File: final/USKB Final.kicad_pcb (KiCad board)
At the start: 2 copper layers, 385.8 x 100 mm, 166 parts, among them SW1 SW_PUSH, U1 ProMicro

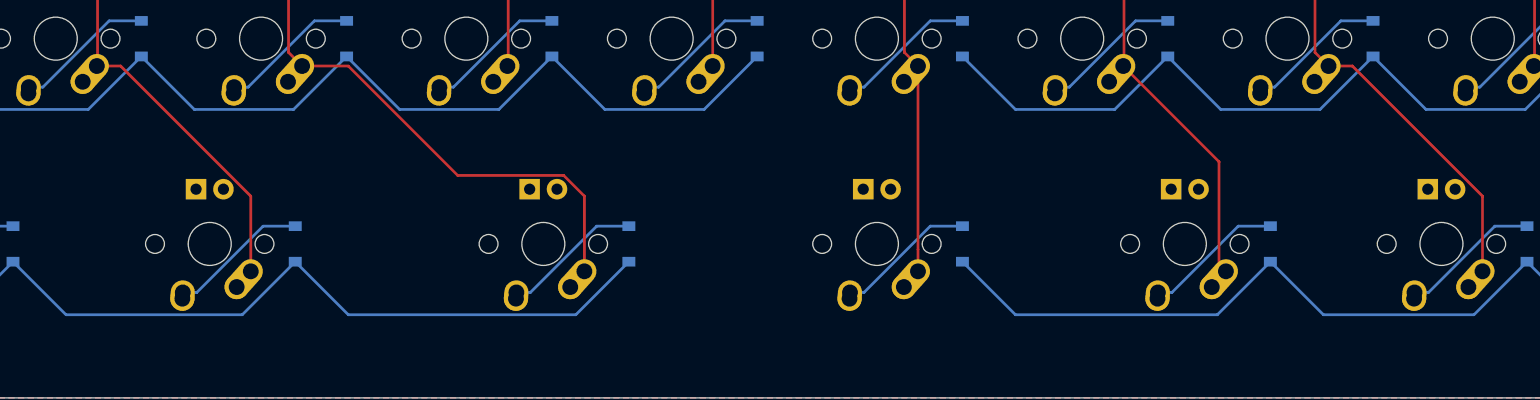
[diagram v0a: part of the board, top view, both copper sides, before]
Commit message: updated footprints and cpl to match cap set
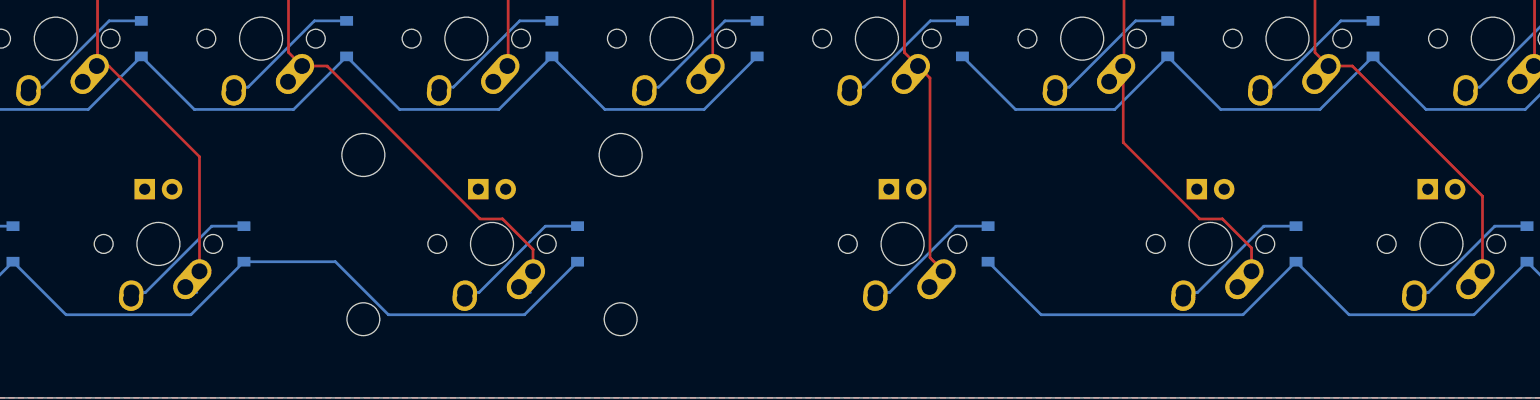
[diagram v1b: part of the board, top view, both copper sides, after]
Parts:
- K_Space1: footprint KeyboardMasterList:MX-1.5U -> Keyboard Master List:MX-1U
- K_Space_2: footprint KeyboardMasterList:MX-1.75U -> Keyboard Master List:MX-2.25U
- K_Space_3: footprint KeyboardMasterList:MX-1.5U -> Keyboard Master List:MX-1.75U
- K_Space_4: footprint KeyboardMasterList:MX-1.5U -> Keyboard Master List:MX-1.25U
- moved D_Space1 4.76 mm to (155.6, 112.7)
- moved K_Space1 4.76 mm to (147.6, 112.7)
- moved D_Space_2 4.76 mm to (186.5, 112.7)
- moved K_Space_2 4.76 mm to (178.6, 112.7)
- moved D_Space_4 2.38 mm to (253.2, 112.7)
- moved K_Space_4 2.38 mm to (245.3, 112.7)
- moved D_Space_3 2.38 mm to (224.6, 112.7)
- moved K_Space_3 2.38 mm to (216.7, 112.7)
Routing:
- net L_COL4: track 215.6 -> 209.3 mm
- net L_ROW4: track 245.2 -> 240.5 mm
- net ROW4: track 265.6 -> 263.2 mm
- net L_COL3: track 185.6 -> 184.3 mm
- net COL0: track 269.7 -> 270.7 mm
- net COL1: track 254.7 -> 255.5 mm

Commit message: made cad for plate, made gerbers and a bunch of other stuff
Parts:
- moved L_OL1 7.94 mm to (31.8, 66.7), turned to 180 degrees
- moved OL1 7.94 mm to (395.3, 66.7), turned to 180 degrees
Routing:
- net SDA: track 30.5 -> 33.4 mm
- net L_SDA: track 33.4 -> 30.6 mm
- net SCL: track 27.0 -> 25.8 mm
- net L_SCL: track 25.8 -> 27.0 mm
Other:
- board text added: "JLCJLCJLCJLC"
